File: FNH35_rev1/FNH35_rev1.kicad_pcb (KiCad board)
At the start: 2 copper layers, 126.2 x 116.7 mm, 116 parts, among them J1 Conn_01x03, J2 Conn_01x08, J3 DX07B024JJ3R1600, K0 KEYSW, K1 KEYSW, K10 KEYSW, K11 KEYSW, K12 KEYSW, K2 KEYSW, K20 KEYSW, K21 KEYSW, K22 KEYSW, K23 KEYSW, K30 KEYSW, K31 KEYSW, K32 KEYSW, K33 KEYSW, K40 KEYSW, K41 KEYSW, K42 KEYSW, K43 KEYSW, SW1 SW_PUSH, U1 STM32F303CCTx, U2 LD1117S33TR_SOT223, U3 74AHCT125, X1 XTAL_GND

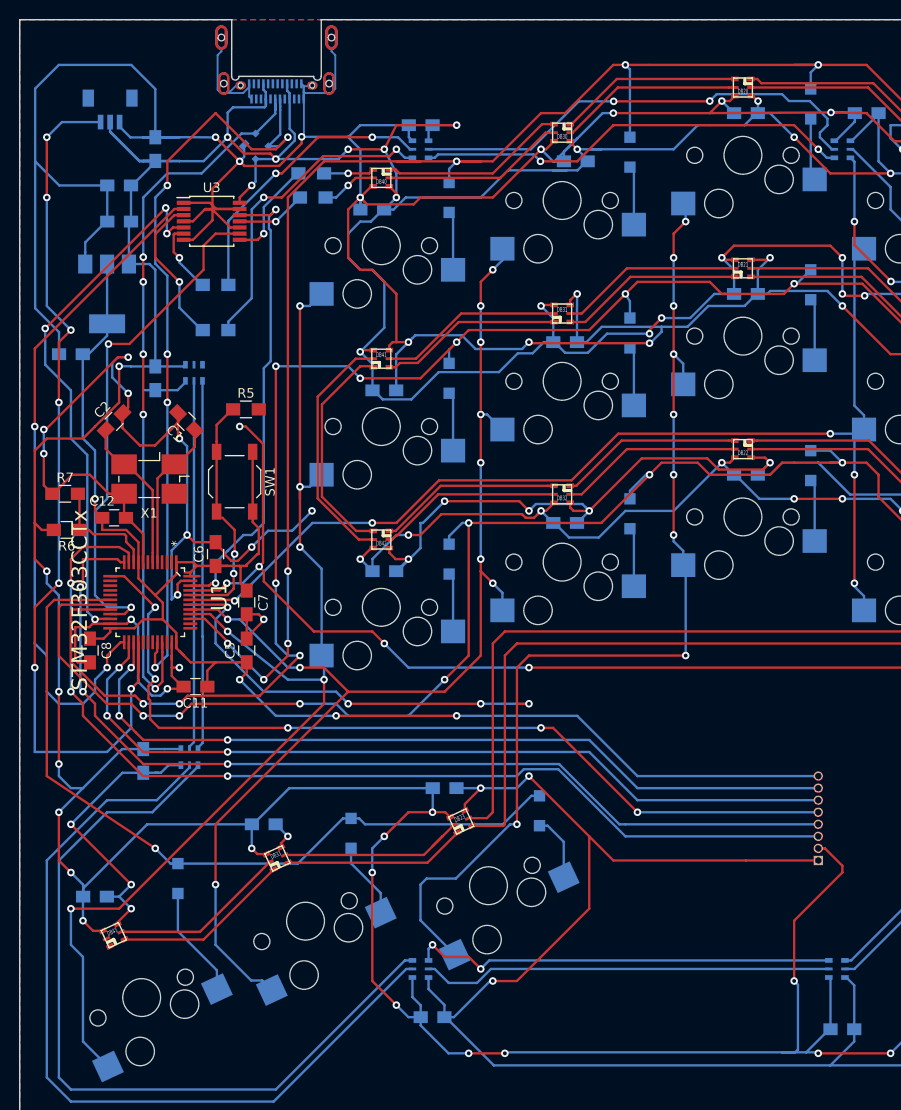
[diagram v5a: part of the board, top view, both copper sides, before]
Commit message: redoing wiring, deleted shitty stuff
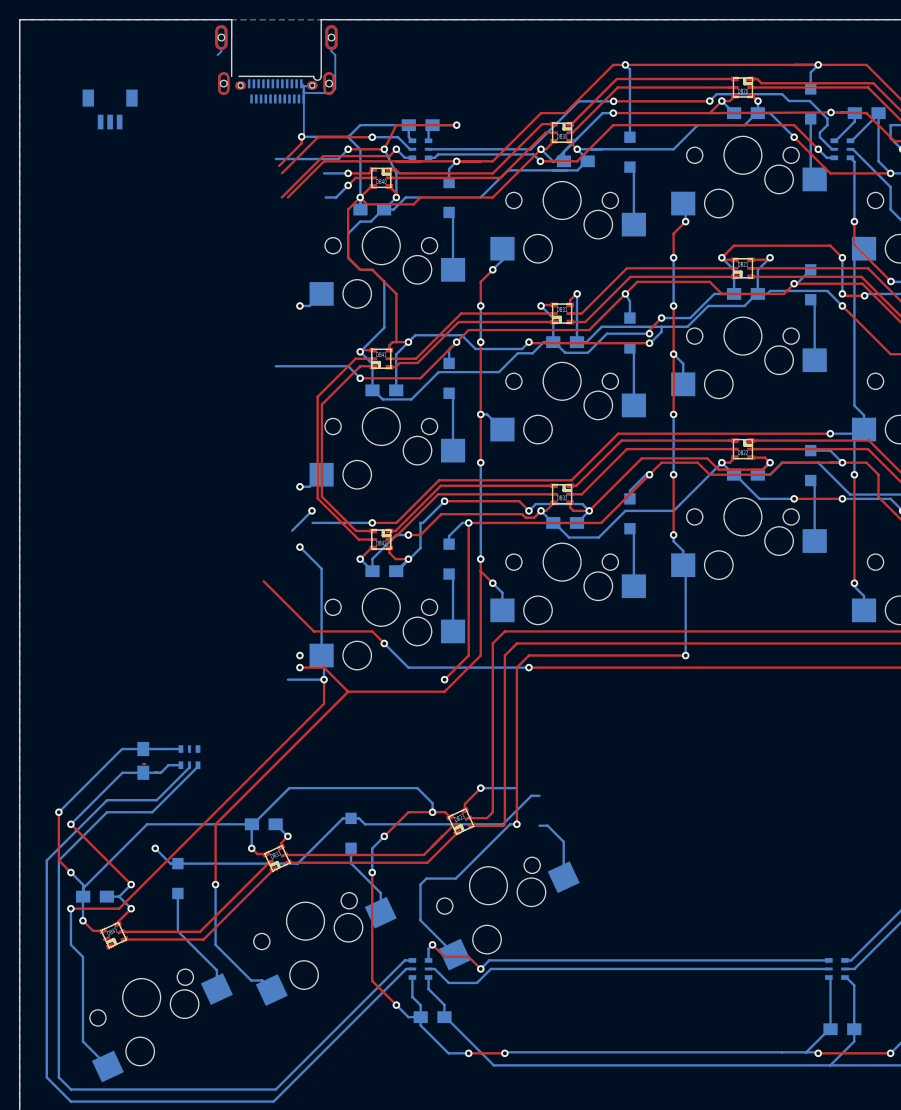
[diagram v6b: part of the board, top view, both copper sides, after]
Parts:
- removed C1, C2: 33pf, Capacitors_SMD:C_0805_HandSoldering
- removed C10, C4, C9: 10u, Capacitors_SMD:C_0805_HandSoldering
- removed C11: 4.7u, Capacitors_SMD:C_0805_HandSoldering
- removed C12: 1u, Capacitors_SMD:C_0805_HandSoldering
- removed C3: 100n, Capacitors_SMD:C_0805_HandSoldering
- removed C5, C6, C7, C8, CB23, CU5: 0.1u, Capacitors_SMD:C_0805_HandSoldering
- removed D1: PRTR5V0U2X,215, tm-kicad-lib:PRTR5V0U2X,215
- removed DS23: D, keyboard_parts:D_SOD123_hand
- removed DU8: APA102, gsg-modules:APA102-2020
- removed J2: Conn_01x08, Pin_Headers:Pin_Header_Angled_1x08_Pitch1.27mm
- removed R1, R2, R3, R4: 300, Resistors_SMD:R_0805_HandSoldering
- removed R5: 10kR, Resistors_SMD:R_0805_HandSoldering
- removed R6: 4k1, Resistors_SMD:R_0805_HandSoldering
- removed R7: 9k1, Resistors_SMD:R_0805_HandSoldering
- removed SW1: SW_PUSH, Buttons_Switches_SMD:SW_SPST_TL3342
- removed U1: STM32F303CCTx, QFP50P900X900X160-48N:QFP50P900X900X160-48N
- removed U2: LD1117S33TR_SOT223, TO_SOT_Packages_SMD:SOT-223-3_TabPin2
- removed U3: 74AHCT125, Housings_SSOP:TSSOP-14_4.4x5mm_Pitch0.65mm
- removed X1: XTAL_GND, Crystals:Crystal_SMD_0603-4pin_6.0x3.5mm_HandSoldering
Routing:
- net GND: track 966.1 -> 633.5 mm, vias 54 -> 38
- net +5V: track 848.1 -> 673.1 mm, vias 52 -> 44
- net +3V3: track 168.0 -> 0.00 mm, vias 4 -> 0
- net Net-(J2-Pad3): track 108.1 -> 0.00 mm, vias 3 -> 0
- net Net-(J2-Pad4): track 102.7 -> 0.20 mm, vias 3 -> 0
- net /SerConn: track 97.4 -> 0.00 mm, vias 7 -> 0
- net Net-(J2-Pad5): track 93.3 -> 0.00 mm, vias 5 -> 0
- net /PB13: track 87.3 -> 0.00 mm, vias 3 -> 0
- net /PB14: track 85.2 -> 0.00 mm, vias 3 -> 0
- net /DA-: track 83.3 -> 0.00 mm, vias 5 -> 0
- net /DA+: track 78.4 -> 0.00 mm, vias 5 -> 0
- net Net-(U1-Pad25): track 71.3 -> 0.00 mm, vias 2 -> 0
- net /SwitchMatrix/row1: track 184.8 -> 114.8 mm, vias 11 -> 7
- net /SwitchMatrix/row0: track 192.5 -> 130.1 mm, vias 9 -> 5
- net Net-(U1-Pad22): track 57.2 -> 0.00 mm, vias 4 -> 0
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
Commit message: before mirror attempts
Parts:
- added C1: 33pf, Capacitors_SMD:C_0805_HandSoldering, F.Cu at (80.2, 95.2)
- added C10: 10u, Capacitors_SMD:C_0805_HandSoldering, F.Cu at (111.9, 124.5)
- added C11: 4.7u, Capacitors_SMD:C_0805_HandSoldering, F.Cu at (105.6, 106.7)
- added C12: 1u, Capacitors_SMD:C_0805_HandSoldering, F.Cu at (89.1, 97.8)
- added C2: 33pf, Capacitors_SMD:C_0805_HandSoldering, F.Cu at (80.2, 106.7)
- added C3: 100n, Capacitors_SMD:C_0805_HandSoldering, F.Cu at (115.7, 113.0)
- added C4: 10u, Capacitors_SMD:C_0805_HandSoldering, F.Cu at (110.6, 106.7)
- added C5: 0.1u, Capacitors_SMD:C_0805_HandSoldering, F.Cu at (101.8, 108.0)
- added C6: 0.1u, Capacitors_SMD:C_0805_HandSoldering, F.Cu at (103.0, 95.2)
- added C7: 0.1u, Capacitors_SMD:C_0805_HandSoldering, F.Cu at (86.9, 107.6)
- added C8: 0.1u, Capacitors_SMD:C_0805_HandSoldering, F.Cu at (89.1, 91.4)
- added C9: 10u, Capacitors_SMD:C_0805_HandSoldering, F.Cu at (118.3, 110.5)
- added CB23: 0.1u, Capacitors_SMD:C_0805_HandSoldering, B.Cu at (62.4, 99.1)
- added CU5: 0.1u, Capacitors_SMD:C_0805_HandSoldering, B.Cu at (30.6, 58.4)
- added D1: PRTR5V0U2X,215, tm-kicad-lib:PRTR5V0U2X,215, B.Cu at (42.8, 37.3)
- added DS23: D, keyboard_parts:D_SOD123_hand, B.Cu at (71.3, 102.6)
- added DU8: APA102, gsg-modules:APA102-2020, B.Cu at (34.4, 58.4)
- added J2: Conn_01x08, Pin_Headers:Pin_Header_Angled_1x08_Pitch1.27mm, B.Cu at (110.6, 94.0)
- added R1: 300, Resistors_SMD:R_0805_HandSoldering, F.Cu at (38.2, 50.8)
- added R2: 300, Resistors_SMD:R_0805_HandSoldering, F.Cu at (33.1, 52.0)
- added R3: 300, Resistors_SMD:R_0805_HandSoldering, F.Cu at (33.1, 33.0)
- added R4: 300, Resistors_SMD:R_0805_HandSoldering, F.Cu at (35.7, 35.5)
- added R5: 10kR, Resistors_SMD:R_0805_HandSoldering, F.Cu at (95.4, 118.1)
- added R6: 4k1, Resistors_SMD:R_0805_HandSoldering, F.Cu at (89.1, 110.5)
- added R7: 9k1, Resistors_SMD:R_0805_HandSoldering, F.Cu at (90.3, 113.0)
- added SW1: SW_PUSH, Buttons_Switches_SMD:SW_SPST_TL3342, B.Cu at (87.8, 123.2)
- added U1: STM32F303CCTx, QFP50P900X900X160-48N:QFP50P900X900X160-48N, F.Cu at (95.8, 101.3)
- added U2: LD1117S33TR_SOT223, TO_SOT_Packages_SMD:SOT-223-3_TabPin2, F.Cu at (109.4, 114.3)
- added U3: 74AHCT125, Housings_SSOP:TSSOP-14_4.4x5mm_Pitch0.65mm, F.Cu at (33.1, 44.4)
- added X1: XTAL_GND, Crystals:Crystal_SMD_0603-4pin_6.0x3.5mm_HandSoldering, F.Cu at (84.0, 101.0)
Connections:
- net /SwitchMatrix/col0 renamed /col0
- net /SwitchMatrix/col1 renamed /col1
- net /SwitchMatrix/col2 renamed /col2
- net /SwitchMatrix/col3 renamed /col3
- net /SwitchMatrix/col4 renamed /col4
- net /SwitchMatrix/row0 renamed /row0
- net /SwitchMatrix/row1 renamed /row1
- net /SwitchMatrix/row2 renamed /row2
- net /SwitchMatrix/row3 renamed /row3
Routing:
- net GND: track 633.5 -> 1026.3 mm, vias 38 -> 44
- net +5V: track 673.1 -> 1063.4 mm, vias 44 -> 57
- net /SerConn: track 0.00 -> 257.2 mm, vias 0 -> 1
- net +3V3: track 0.00 -> 168.5 mm, vias 0 -> 9
- net /SDI_Und: track 0.00 -> 156.2 mm, vias 0 -> 6
- net /CKI_Und: track 0.00 -> 155.4 mm, vias 0 -> 4
- net /DA+: track 0.00 -> 151.7 mm, vias 0 -> 5
- net /SDI_Back: track 0.00 -> 150.5 mm, vias 0 -> 6
- net /CKI_Back: track 0.00 -> 145.0 mm, vias 0 -> 8
- net /DA-: track 0.00 -> 143.0 mm, vias 0 -> 5
- net /BOOT: track 0.00 -> 88.5 mm, vias 0 -> 8
- net /col4: track 80.8 -> 165.2 mm
- net /row0: track 130.1 -> 193.1 mm, vias 5 -> 12
- net /row1: track 114.8 -> 175.7 mm, vias 7 -> 5
- net /col3: track 113.9 -> 160.6 mm, vias 9 -> 10
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
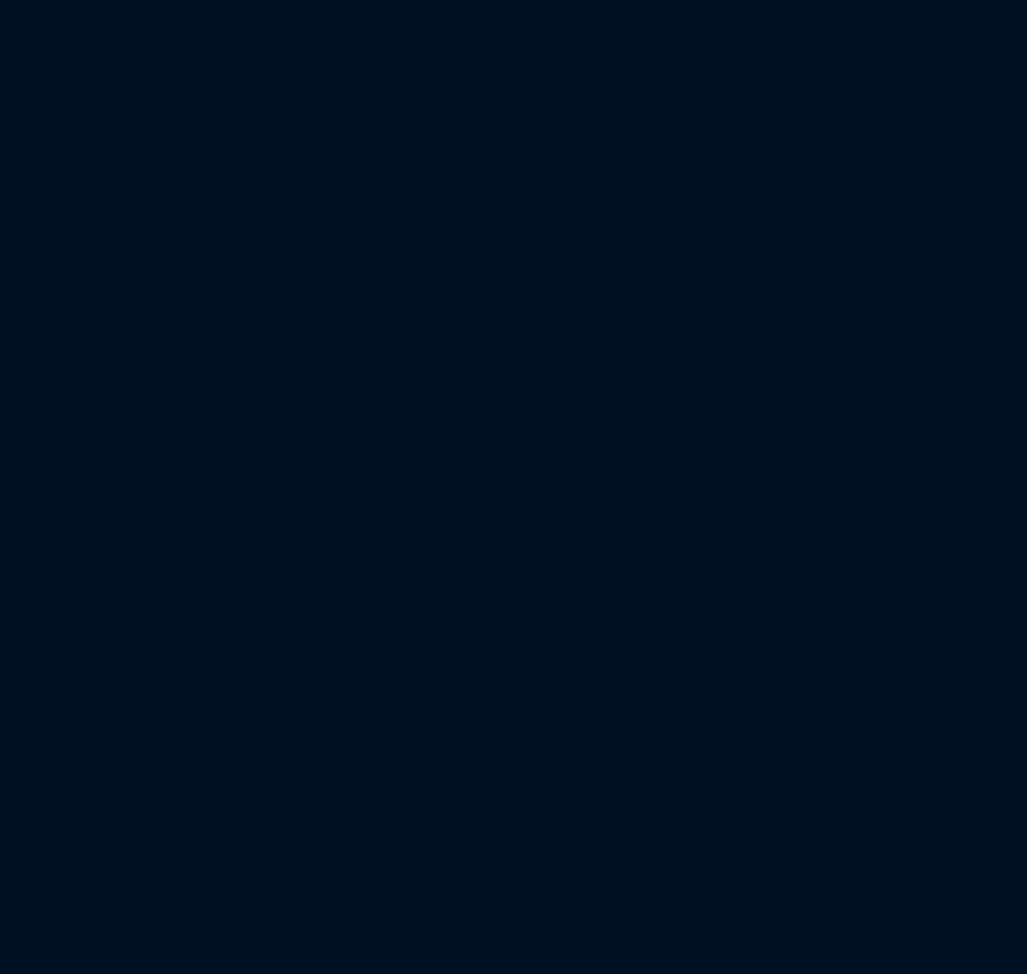
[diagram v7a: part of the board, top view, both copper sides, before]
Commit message: mirrored PCB: success
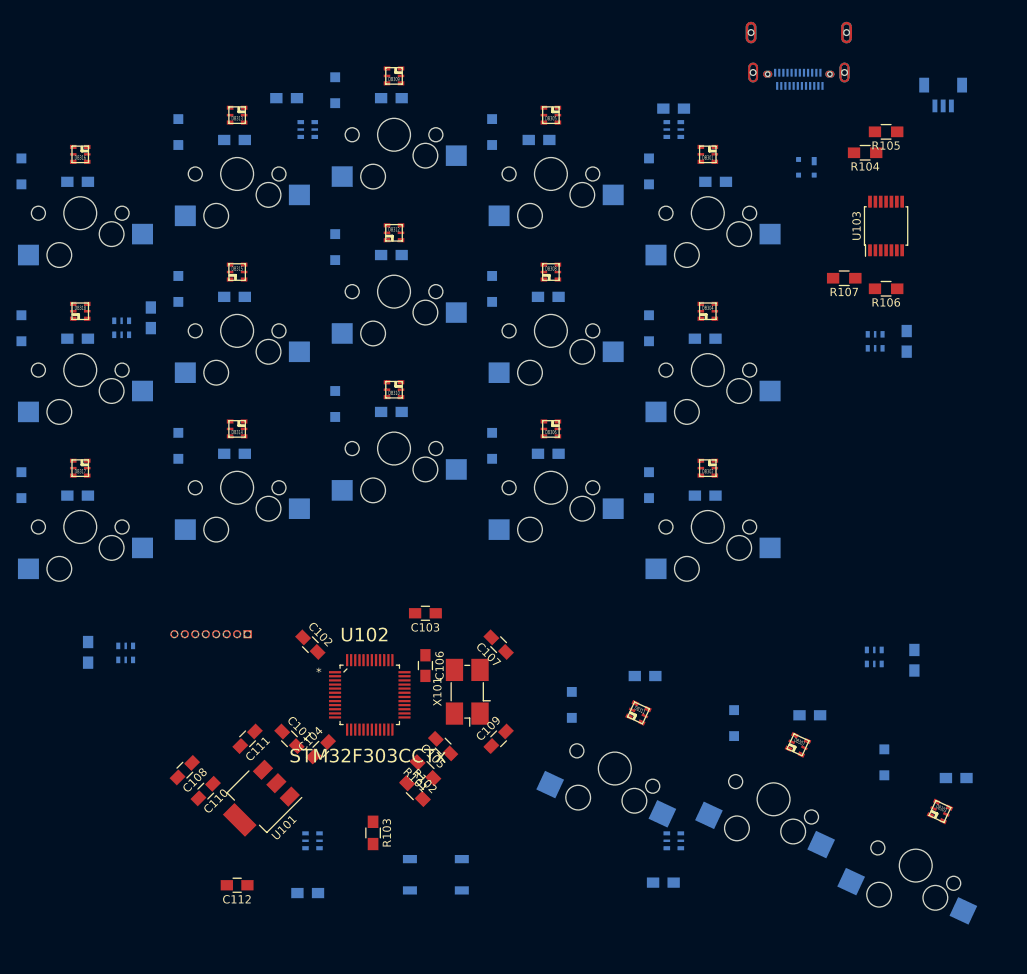
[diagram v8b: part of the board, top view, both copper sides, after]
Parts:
- added C101: 4.7u, Capacitors_SMD:C_0805_HandSoldering, F.Cu at (-73.6, 106.7)
- added C102: 0.1u, Capacitors_SMD:C_0805_HandSoldering, F.Cu at (-71.0, 95.2)
- added C103: 0.1u, Capacitors_SMD:C_0805_HandSoldering, F.Cu at (-57.1, 91.4)
- added C104: 0.1u, Capacitors_SMD:C_0805_HandSoldering, F.Cu at (-69.8, 108.0)
- added C105: 0.1u, Capacitors_SMD:C_0805_HandSoldering, F.Cu at (-54.9, 107.6)
- added C106: 1u, Capacitors_SMD:C_0805_HandSoldering, F.Cu at (-57.1, 97.8)
- added C107: 33pf, Capacitors_SMD:C_0805_HandSoldering, F.Cu at (-48.2, 95.2)
- added C108: 10u, Capacitors_SMD:C_0805_HandSoldering, F.Cu at (-86.3, 110.5)
- added C109: 33pf, Capacitors_SMD:C_0805_HandSoldering, F.Cu at (-48.2, 106.7)
- added C110: 100n, Capacitors_SMD:C_0805_HandSoldering, F.Cu at (-83.7, 113.0)
- added C111: 10u, Capacitors_SMD:C_0805_HandSoldering, F.Cu at (-78.6, 106.7)
- added C112: 10u, Capacitors_SMD:C_0805_HandSoldering, F.Cu at (-79.9, 124.5)
- added CB301: 0.1u, Capacitors_SMD:C_0805_HandSoldering, B.Cu at (-21.8, 39.1)
- added CB302: 0.1u, Capacitors_SMD:C_0805_HandSoldering, B.Cu at (-23.1, 77.2)
- added CB303: 0.1u, Capacitors_SMD:C_0805_HandSoldering, B.Cu at (7.39, 111.4)
- added CB304: 0.1u, Capacitors_SMD:C_0805_HandSoldering, B.Cu at (-23.1, 58.1)
- added CB305: 0.1u, Capacitors_SMD:C_0805_HandSoldering, B.Cu at (-43.3, 34.0)
- added CB306: 0.1u, Capacitors_SMD:C_0805_HandSoldering, B.Cu at (-42.1, 72.1)
- added CB307: 0.1u, Capacitors_SMD:C_0805_HandSoldering, B.Cu at (-10.4, 103.8)
- added CB308: 0.1u, Capacitors_SMD:C_0805_HandSoldering, B.Cu at (-42.1, 53.0)
- added CB309: 0.1u, Capacitors_SMD:C_0805_HandSoldering, B.Cu at (-61.2, 28.9)
- added CB310: 0.1u, Capacitors_SMD:C_0805_HandSoldering, B.Cu at (-61.2, 67.0)
- added CB311: 0.1u, Capacitors_SMD:C_0805_HandSoldering, B.Cu at (-30.4, 99.1)
- added CB312: 0.1u, Capacitors_SMD:C_0805_HandSoldering, B.Cu at (-61.2, 47.9)
- added CB313: 0.1u, Capacitors_SMD:C_0805_HandSoldering, B.Cu at (-80.2, 34.0)
- added CB314: 0.1u, Capacitors_SMD:C_0805_HandSoldering, B.Cu at (-80.2, 72.1)
- added CB315: 0.1u, Capacitors_SMD:C_0805_HandSoldering, B.Cu at (-80.2, 53.0)
- added CB316: 0.1u, Capacitors_SMD:C_0805_HandSoldering, B.Cu at (-99.3, 39.1)
- added CB317: 0.1u, Capacitors_SMD:C_0805_HandSoldering, B.Cu at (-99.3, 77.2)
- added CB318: 0.1u, Capacitors_SMD:C_0805_HandSoldering, B.Cu at (-99.3, 58.1)
- added CU401: 0.1u, Capacitors_SMD:C_0805_HandSoldering, B.Cu at (1.38, 58.4)
- added CU402: 0.1u, Capacitors_SMD:C_0805_HandSoldering, B.Cu at (2.31, 97.1)
- added CU403: 0.1u, Capacitors_SMD:C_0805_HandSoldering, B.Cu at (-26.9, 30.2)
- added CU404: 0.1u, Capacitors_SMD:C_0805_HandSoldering, B.Cu at (-28.2, 124.1)
- added CU405: 0.1u, Capacitors_SMD:C_0805_HandSoldering, B.Cu at (-73.9, 28.9)
- added CU406: 0.1u, Capacitors_SMD:C_0805_HandSoldering, B.Cu at (-71.3, 125.4)
- added CU407: 0.1u, Capacitors_SMD:C_0805_HandSoldering, B.Cu at (-90.4, 55.6)
- added CU408: 0.1u, Capacitors_SMD:C_0805_HandSoldering, B.Cu at (-98.0, 96.2)
- added D101: PRTR5V0U2X,215, tm-kicad-lib:PRTR5V0U2X,215, B.Cu at (-10.8, 37.3)
- added DB301: APA102, gsg-modules:APA102-2020, F.Cu at (-22.8, 35.7)
- added DB302: APA102, gsg-modules:APA102-2020, F.Cu at (-22.8, 73.8)
- added DB303: APA102, gsg-modules:APA102-2020, F.Cu at (5.42, 115.5)
- added DB304: APA102, gsg-modules:APA102-2020, F.Cu at (-22.8, 54.8)
- added DB305: APA102, gsg-modules:APA102-2020, F.Cu at (-41.8, 31.0)
- added DB306: APA102, gsg-modules:APA102-2020, F.Cu at (-41.8, 69.1)
- added DB307: APA102, gsg-modules:APA102-2020, F.Cu at (-11.8, 107.4)
- added DB308: APA102, gsg-modules:APA102-2020, F.Cu at (-41.8, 50.0)
- added DB309: APA102, gsg-modules:APA102-2020, F.Cu at (-60.9, 26.2)
- added DB310: APA102, gsg-modules:APA102-2020, F.Cu at (-60.9, 64.3)
- added DB311: APA102, gsg-modules:APA102-2020, F.Cu at (-31.2, 103.5)
- added DB312: APA102, gsg-modules:APA102-2020, F.Cu at (-60.9, 45.2)
- added DB313: APA102, gsg-modules:APA102-2020, F.Cu at (-79.9, 31.0)
- added DB314: APA102, gsg-modules:APA102-2020, F.Cu at (-79.9, 69.1)
- added DB315: APA102, gsg-modules:APA102-2020, F.Cu at (-79.9, 50.0)
- added DB316: APA102, gsg-modules:APA102-2020, F.Cu at (-99.0, 35.7)
- added DB317: APA102, gsg-modules:APA102-2020, F.Cu at (-99.0, 73.8)
- added DB318: APA102, gsg-modules:APA102-2020, F.Cu at (-99.0, 54.8)
- added DR401: APA102, gsg-modules:APA102-2020, B.Cu at (-2.45, 58.4)
- added DR402: APA102, gsg-modules:APA102-2020, B.Cu at (-2.55, 96.7)
- added DR403: APA102, gsg-modules:APA102-2020, B.Cu at (-26.9, 32.7)
- added DR404: APA102, gsg-modules:APA102-2020, B.Cu at (-26.9, 119.1)
- added DR405: APA102, gsg-modules:APA102-2020, B.Cu at (-71.3, 32.7)
- added DR406: APA102, gsg-modules:APA102-2020, B.Cu at (-70.8, 119.1)
- added DR407: APA102, gsg-modules:APA102-2020, B.Cu at (-93.9, 56.8)
- added DR408: APA102, gsg-modules:APA102-2020, B.Cu at (-93.5, 96.3)
- added DS201: D, keyboard_parts:D_SOD123_hand, B.Cu at (-29.9, 37.8)
- added DS202: D, keyboard_parts:D_SOD123_hand, B.Cu at (-29.9, 56.8)
- added DS203: D, keyboard_parts:D_SOD123_hand, B.Cu at (-29.9, 75.9)
- added DS204: D, keyboard_parts:D_SOD123_hand, B.Cu at (-1.34, 109.5)
- added DS205: D, keyboard_parts:D_SOD123_hand, B.Cu at (-49.0, 33.0)
- added DS206: D, keyboard_parts:D_SOD123_hand, B.Cu at (-49.0, 52.1)
- added DS207: D, keyboard_parts:D_SOD123_hand, B.Cu at (-49.0, 71.1)
- added DS208: D, keyboard_parts:D_SOD123_hand, B.Cu at (-19.6, 104.8)
- added DS209: D, keyboard_parts:D_SOD123_hand, B.Cu at (-68.0, 27.9)
- added DS210: D, keyboard_parts:D_SOD123_hand, B.Cu at (-68.0, 47.0)
- added DS211: D, keyboard_parts:D_SOD123_hand, B.Cu at (-68.0, 66.0)
- added DS212: D, keyboard_parts:D_SOD123_hand, B.Cu at (-39.3, 102.6)
- added DS213: D, keyboard_parts:D_SOD123_hand, B.Cu at (-87.1, 33.0)
- added DS214: D, keyboard_parts:D_SOD123_hand, B.Cu at (-87.1, 52.1)
- added DS215: D, keyboard_parts:D_SOD123_hand, B.Cu at (-87.1, 71.1)
- added DS216: D, keyboard_parts:D_SOD123_hand, B.Cu at (-106.1, 37.8)
- added DS217: D, keyboard_parts:D_SOD123_hand, B.Cu at (-106.1, 56.8)
- added DS218: D, keyboard_parts:D_SOD123_hand, B.Cu at (-106.1, 75.9)
- added J101: Conn_01x03, Connectors_JST:JST_SH_BM03B-SRSS-TB_03x1.00mm_Straight, B.Cu at (5.81, 28.6)
- added J102: DX07B024JJ3R1600, butts:JAE_DX07B024JJ3R1600, B.Cu at (-11.7, 25.8)
- added J103: Conn_01x08, Pin_Headers:Pin_Header_Angled_1x08_Pitch1.27mm, B.Cu at (-78.6, 94.0)
- added K201: KEYSW, keyswitches:Kailh_socket, F.Cu at (-22.8, 42.9)
- added K202: KEYSW, keyswitches:Kailh_socket, F.Cu at (-22.8, 61.9)
- added K203: KEYSW, keyswitches:Kailh_socket, F.Cu at (-22.8, 81.0)
- added K204: KEYSW, keyswitches:Kailh_socket, F.Cu at (2.48, 122.1)
- added K205: KEYSW, keyswitches:Kailh_socket, F.Cu at (-41.8, 38.1)
- added K206: KEYSW, keyswitches:Kailh_socket, F.Cu at (-41.8, 57.1)
- added K207: KEYSW, keyswitches:Kailh_socket, F.Cu at (-41.8, 76.2)
- added K208: KEYSW, keyswitches:Kailh_socket, F.Cu at (-14.8, 114.0)
- added K209: KEYSW, keyswitches:Kailh_socket, F.Cu at (-60.9, 33.3)
- added K210: KEYSW, keyswitches:Kailh_socket, F.Cu at (-60.9, 52.4)
- added K211: KEYSW, keyswitches:Kailh_socket, F.Cu at (-60.9, 71.4)
- added K212: KEYSW, keyswitches:Kailh_socket, F.Cu at (-34.1, 110.3)
- added K213: KEYSW, keyswitches:Kailh_socket, F.Cu at (-79.9, 38.1)
- added K214: KEYSW, keyswitches:Kailh_socket, F.Cu at (-79.9, 57.1)
- added K215: KEYSW, keyswitches:Kailh_socket, F.Cu at (-79.9, 76.2)
- added K216: KEYSW, keyswitches:Kailh_socket, F.Cu at (-99.0, 42.9)
- added K217: KEYSW, keyswitches:Kailh_socket, F.Cu at (-99.0, 61.9)
- added K218: KEYSW, keyswitches:Kailh_socket, F.Cu at (-99.0, 81.0)
- added R101: 4k1, Resistors_SMD:R_0805_HandSoldering, F.Cu at (-57.1, 110.5)
- added R102: 9k1, Resistors_SMD:R_0805_HandSoldering, F.Cu at (-58.3, 113.0)
- added R103: 10kR, Resistors_SMD:R_0805_HandSoldering, F.Cu at (-63.4, 118.1)
- added R104: 300, Resistors_SMD:R_0805_HandSoldering, F.Cu at (-3.66, 35.5)
- added R105: 300, Resistors_SMD:R_0805_HandSoldering, F.Cu at (-1.12, 33.0)
- added R106: 300, Resistors_SMD:R_0805_HandSoldering, F.Cu at (-1.12, 52.0)
- added R107: 300, Resistors_SMD:R_0805_HandSoldering, F.Cu at (-6.20, 50.8)
- added SW101: SW_PUSH, Buttons_Switches_SMD:SW_SPST_TL3342, B.Cu at (-55.8, 123.2)
- added U101: LD1117S33TR_SOT223, TO_SOT_Packages_SMD:SOT-223-3_TabPin2, F.Cu at (-77.4, 114.3)
- added U102: STM32F303CCTx, QFP50P900X900X160-48N:QFP50P900X900X160-48N, F.Cu at (-63.8, 101.3)
- added U103: 74AHCT125, Housings_SSOP:TSSOP-14_4.4x5mm_Pitch0.65mm, F.Cu at (-1.12, 44.4)
- added X101: XTAL_GND, Crystals:Crystal_SMD_0603-4pin_6.0x3.5mm_HandSoldering, F.Cu at (-52.0, 101.0)
